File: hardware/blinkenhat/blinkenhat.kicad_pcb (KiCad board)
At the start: 2 copper layers, 0 parts

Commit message: Hardware: update schematics.
Signed-off-by: Jan Losinski <losinski@wh2.tu-dresden.de>
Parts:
- added C1: 100µ, Capacitors_SMD:CP_Elec_6.3x5.8, F.Cu at (162.8, 98.0)
- added C2: 22µ, Capacitors_SMD:CP_Elec_5x5.3, F.Cu at (162.8, 110.0)
- added C3: 100µ, Capacitors_SMD:CP_Elec_6.3x5.8, F.Cu at (141.0, 100.8)
- added C4: 100n, Capacitors_SMD:C_0603, F.Cu at (130.3, 98.8)
- added D1: D, DO214:DO-214AC(SMA), F.Cu at (162.8, 103.4)
- added D2: D, DO214:DO-214AC(SMA), F.Cu at (135.9, 90.2)
- added J1: LED1, Connectors_JST:JST_XH_B03B-XH-A_03x2.50mm_Straight, F.Cu at (149.6, 109.0)
- added J2: LED2, Connectors_JST:JST_XH_B03B-XH-A_03x2.50mm_Straight, F.Cu at (149.6, 100.8)
- added J3: INPUT, Connectors_JST:JST_XH_B03B-XH-A_03x2.50mm_Straight, F.Cu at (149.6, 90.2)
- added J4: Programmer, Pin_Headers:Pin_Header_Straight_2x04_Pitch2.54mm, F.Cu at (130.8, 88.1)
- added J5: USB_POWER, Connectors:USB_Micro-B_10103594-0001LF, F.Cu at (162.8, 89.9)
- added J6: GPIO, Pin_Headers:Pin_Header_Straight_2x05_Pitch1.27mm, F.Cu at (137.9, 109.5)
- added Q1: 2N7002, TO_SOT_Packages_SMD:SOT-23, F.Cu at (118.2, 104.6)
- added Q2: 2N7002, TO_SOT_Packages_SMD:SOT-23, F.Cu at (122.8, 104.6)
- added R1: 10K, Resistors_SMD:R_0603, F.Cu at (121.7, 98.8)
- added R2: 10K, Resistors_SMD:R_0603, F.Cu at (117.6, 98.8)
- added R3: 10K, Resistors_SMD:R_0603, F.Cu at (125.7, 106.9)
- added R4: 10K, Resistors_SMD:R_0603, F.Cu at (127.8, 106.9)
- added R5: 10K, Resistors_SMD:R_0603, F.Cu at (129.8, 106.9)
- added R6: 10K, Resistors_SMD:R_0603, F.Cu at (117.7, 102.1)
- added R7: 3.3K, Resistors_SMD:R_0603, F.Cu at (117.7, 107.2)
- added R8: 10K, Resistors_SMD:R_0603, F.Cu at (122.2, 102.1)
- added R9: 3.3K, Resistors_SMD:R_0603, F.Cu at (122.2, 107.2)
- added SW1: RESET, Buttons_Switches_SMD:SW_SPST_PTS645, F.Cu at (114.6, 89.7)
- added U1: AMS1117-3V3, TO_SOT_Packages_SMD:SOT-223, F.Cu at (142.5, 92.2)
- added U2: ESP-12E, ESP8266:ESP-12E, B.Cu at (117.6, 95.8)
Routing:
- net GND: track 0.00 -> 157.3 mm, vias 0 -> 1
- net +3V3: track 0.00 -> 74.6 mm, vias 0 -> 1
- net +5V: track 0.00 -> 71.7 mm
- net ADC: track 0.00 -> 39.8 mm
- net OUT1: track 0.00 -> 39.7 mm
- net TX: track 0.00 -> 36.8 mm
- net Net-(C2-Pad1): track 0.00 -> 36.3 mm
- net OUT2: track 0.00 -> 35.9 mm, vias 0 -> 1
- net INP2: track 0.00 -> 31.1 mm
- net GPIO2: track 0.00 -> 30.8 mm, vias 0 -> 1
- net INP1: track 0.00 -> 30.7 mm
- net GPIO0: track 0.00 -> 27.5 mm, vias 0 -> 1
- net RX: track 0.00 -> 24.1 mm
- net RESET: track 0.00 -> 23.9 mm, vias 0 -> 1
- net GPIO5: track 0.00 -> 22.4 mm
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- added copper zone on B.Cu, net GND
- added copper zone on F.Cu, net GND
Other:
- board outline added: 58.9 x 27.9 mm
- net class wide added: clearance 0.2, trace_width 0.4, via_dia 0.6, via_drill 0.4
- board text added: "BlinkenHat v1.0 by Retardigrades"

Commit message: Hardware: redesign PCB.
Signed-off-by: Jan Losinski <losinski@wh2.tu-dresden.de>
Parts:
- C1: value 100µ -> 200µ; footprint Capacitors_SMD:CP_Elec_6.3x5.8 -> Capacitors_Tantalum_SMD:CP_Tantalum_Case-C_EIA-6032-28_Reflow
- C2: footprint Capacitors_SMD:CP_Elec_5x5.3 -> Capacitors_Tantalum_SMD:CP_Tantalum_Case-B_EIA-3528-21_Reflow
- C3: footprint Capacitors_SMD:CP_Elec_6.3x5.8 -> Capacitors_Tantalum_SMD:CP_Tantalum_Case-C_EIA-6032-28_Reflow
- U2: moved to F.Cu
- moved R7 33.4 mm to (145.5, 88.6), turned to 270 degrees
- moved R9 28.7 mm to (144.0, 88.6), turned to 270 degrees
- moved Q1 26.4 mm to (143.3, 96.3), turned to 0 degrees
- moved R6 25.5 mm to (143.0, 98.8)
- moved C2 24.7 mm to (151.4, 88.1)
- moved R8 24.4 mm to (142.5, 88.6), turned to 270 degrees
- moved Q2 23.9 mm to (143.3, 92.2), turned to 0 degrees
- moved J5 23.2 mm to (150.2, 109.4), turned to 0 degrees
- moved R3 22.7 mm to (139.2, 88.6)
- moved J4 22.6 mm to (140.2, 108.7)
- moved R4 22.4 mm to (140.7, 88.6)
- moved SW1 21.9 mm to (122.9, 109.9), turned to 0 degrees
- moved D2 21.3 mm to (144.0, 109.8), turned to 270 degrees
- moved R5 19.5 mm to (136.7, 88.6), turned to 270 degrees
- moved R2 16.5 mm to (128.8, 111.0), turned to 270 degrees
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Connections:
- C2 pad 1: Net-(C2-Pad1) -> +3V3
- C3 pad 1: +3V3 -> Net-(C3-Pad1)
- D1 pad 1: Net-(C2-Pad1) -> Net-(C3-Pad1)
- J3 pad 1: INP1 -> INP2
- J3 pad 2: INP2 -> INP1
- J6 pad 1: CSO -> SCLK
- J6 pad 10: MISO -> +3V3
- J6 pad 2: SCLK -> CSO
- J6 pad 3: GPIO5 -> MOSI
- J6 pad 4: MOSI -> GPIO16
- J6 pad 5: GPIO4 -> GPIO10
- J6 pad 6: GPIO10 -> GPIO15
- J6 pad 7: ADC -> GPIO9
- J6 pad 8: GPIO9 -> ADC
- J6 pad 9: +3V3 -> MISO
- U1 pad 3: Net-(C2-Pad1) -> Net-(C3-Pad1)
- U2 pad 13: GPIO4 -> INP1
- U2 pad 14: GPIO5 -> INP2
- U2 pad 4: INP1 -> GPIO16
- U2 pad 5: INP2 -> GPIO15
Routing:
- net +3V3: track 74.6 -> 114.6 mm
- net Net-(C2-Pad1): track 36.3 -> 0.00 mm
- net GPIO5: track 22.4 -> 0.00 mm
- net GPIO16: track 0.00 -> 22.4 mm, vias 0 -> 1
- net GPIO4: track 21.1 -> 0.00 mm
- net GPIO2: track 30.8 -> 50.5 mm
- net GPIO15: track 0.00 -> 19.6 mm, vias 0 -> 1
- net SCLK: track 4.76 -> 21.1 mm, vias 0 -> 1
- net GPIO0: track 27.5 -> 41.6 mm
- net LED2: track 12.9 -> 26.9 mm, vias 1 -> 0
- net Net-(C3-Pad1): track 0.00 -> 11.5 mm
- net MOSI: track 6.86 -> 17.9 mm, vias 0 -> 1
- net LED1: track 17.3 -> 27.9 mm, vias 1 -> 0
- net INP1: track 30.7 -> 41.1 mm, vias 0 -> 1
- net +5V: track 71.7 -> 63.0 mm
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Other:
- board size 58.9 x 27.9 mm -> 49.8 x 27.9 mm

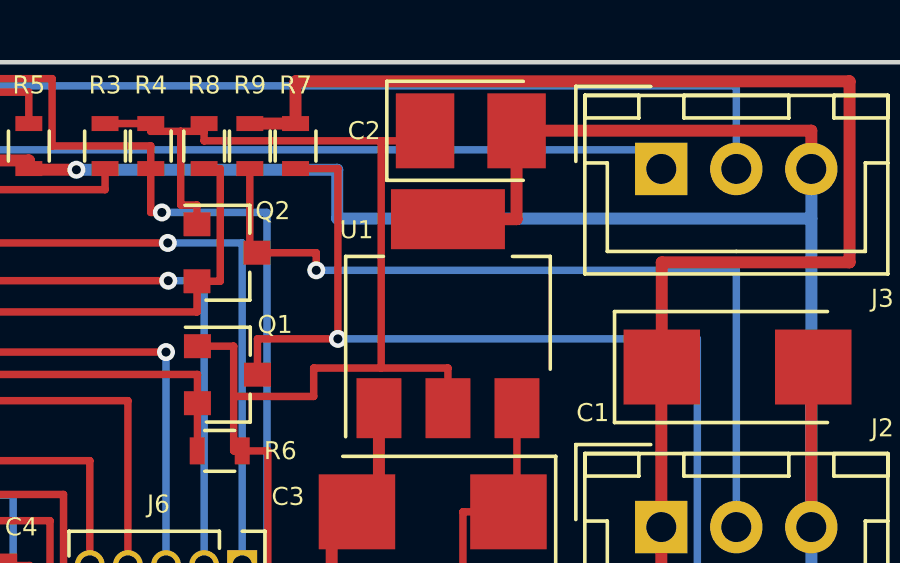
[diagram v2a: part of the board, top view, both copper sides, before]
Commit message: Hardware: fix AMS pad connection.
Signed-off-by: Jan Losinski <losinski@wh2.tu-dresden.de>
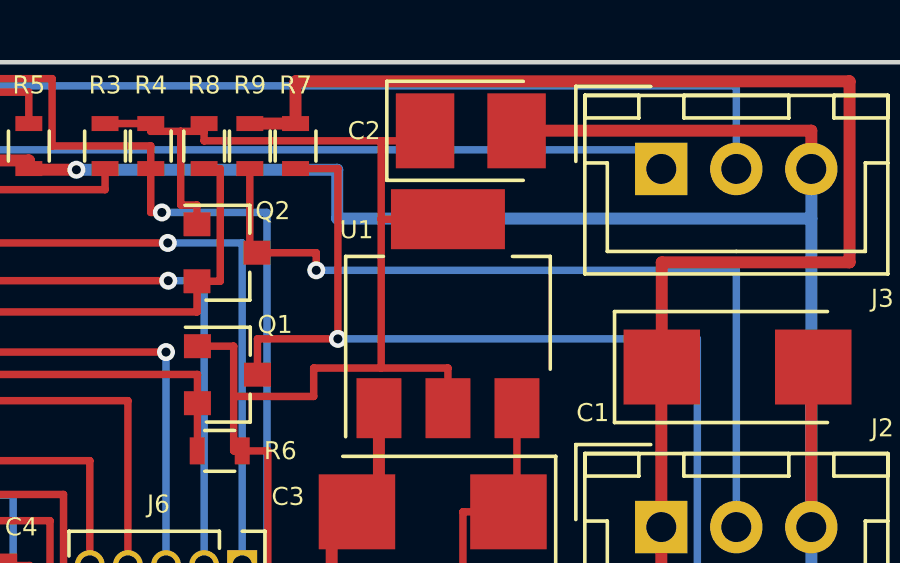
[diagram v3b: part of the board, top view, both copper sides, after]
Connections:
- U1 pad 4: GND -> +3V3
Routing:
- net GND: track 156.9 -> 151.6 mm
- net +3V3: track 114.6 -> 116.8 mm
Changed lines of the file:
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@@
     (links 74)
     (no_connects 0)
-    (area 109.388999 85.776999 190.854001 115.171)
+    (area 116.256999 85.776999 166.191001 113.867001)
     (thickness 1.6)
     (drawings 6)
-    (tracks 253)
+    (tracks 254)
     (zones 0)
     (modules 26)
@@
   (layers
     (0 F.Cu signal)
-    (31 B.Cu signal)
+    (31 B.Cu signal hide)
     (32 B.Adhes user)
     (33 F.Adhes user)
@@
     (fp_line (start 1.85 -3.35) (end 1.85 3.35) (layer F.Fab) (width 0.1))
     (pad 4 smd rect (at 3.15 0 90) (size 2 3.8) (layers F.Cu F.Paste F.Mask)
-      (net 2 GND))
+      (net 3 +3V3))
     (pad 2 smd rect (at -3.15 0 90) (size 2 1.5) (layers F.Cu F.Paste F.Mask)
       (net 3 +3V3))
@@
   (segment (start 162.734 101.346) (end 162.734 109.474) (width 0.4) (layer B.Cu) (net 2))
   (segment (start 126.832 112.196) (end 118.872 112.196) (width 0.4) (layer F.Cu) (net 2))
-  (segment (start 152.909 91.084) (end 150.622 91.084) (width 0.4) (layer F.Cu) (net 2))
-  (segment (start 152.909 88.138) (end 152.909 91.084) (width 0.4) (layer F.Cu) (net 2))
   (segment (start 152.909 88.1326) (end 152.909 88.138) (width 0.4) (layer F.Cu) (net 2))
   (segment (start 162.734 88.1326) (end 152.909 88.1326) (width 0.4) (layer F.Cu) (net 2))
@@
   (segment (start 126.832 110.2055) (end 126.832 112.196) (width 0.4) (layer F.Cu) (net 2))
   (segment (start 126.5231 110.2055) (end 126.832 110.2055) (width 0.4) (layer F.Cu) (net 2))
+  (segment (start 150.622 91.084) (end 148.3966 91.084) (width 0.25) (layer F.Cu) (net 3))
+  (segment (start 148.3966 91.084) (end 148.3966 91.0844) (width 0.25) (layer F.Cu) (net 3))
   (via (at 120.8113 109.208) (size 0.6) (layers F.Cu B.Cu) (net 3))
   (segment (start 140.716 87.896) (end 139.192 87.896) (width 0.25) (layer F.Cu) (net 3))
@@
   (segment (start 150.622 96.0447) (end 148.3966 96.0447) (width 0.25) (layer F.Cu) (net 3))
   (segment (start 150.622 97.384) (end 150.622 96.0447) (width 0.25) (layer F.Cu) (net 3))
-  (segment (start 148.3966 88.4714) (end 148.3966 96.0447) (width 0.25) (layer F.Cu) (net 3))
+  (segment (start 148.3966 88.4714) (end 148.3966 91.0844) (width 0.25) (layer F.Cu) (net 3))
+  (segment (start 148.3966 91.0844) (end 148.3966 96.0447) (width 0.25) (layer F.Cu) (net 3))
   (segment (start 149.859 88.4714) (end 148.3966 88.4714) (width 0.25) (layer F.Cu) (net 3))
   (segment (start 149.859 88.138) (end 149.859 88.4714) (width 0.25) (layer F.Cu) (net 3))
